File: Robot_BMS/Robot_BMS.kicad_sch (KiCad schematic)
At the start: 0 parts

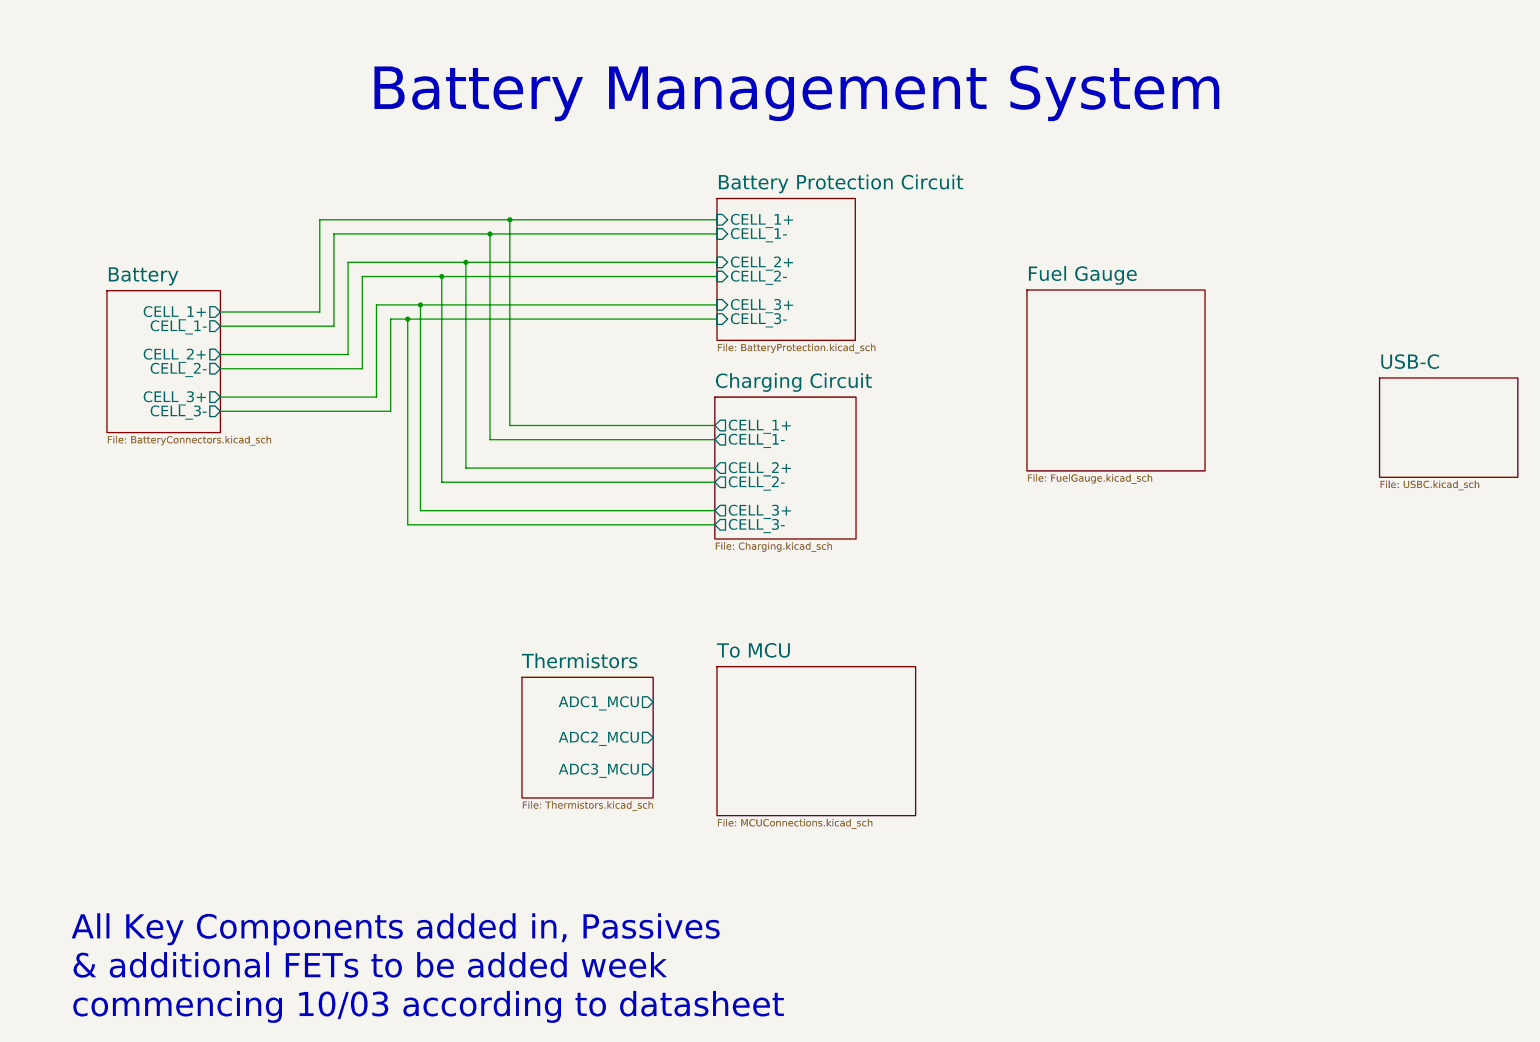
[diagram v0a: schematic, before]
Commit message: DC power supply added via dc Barrel jack
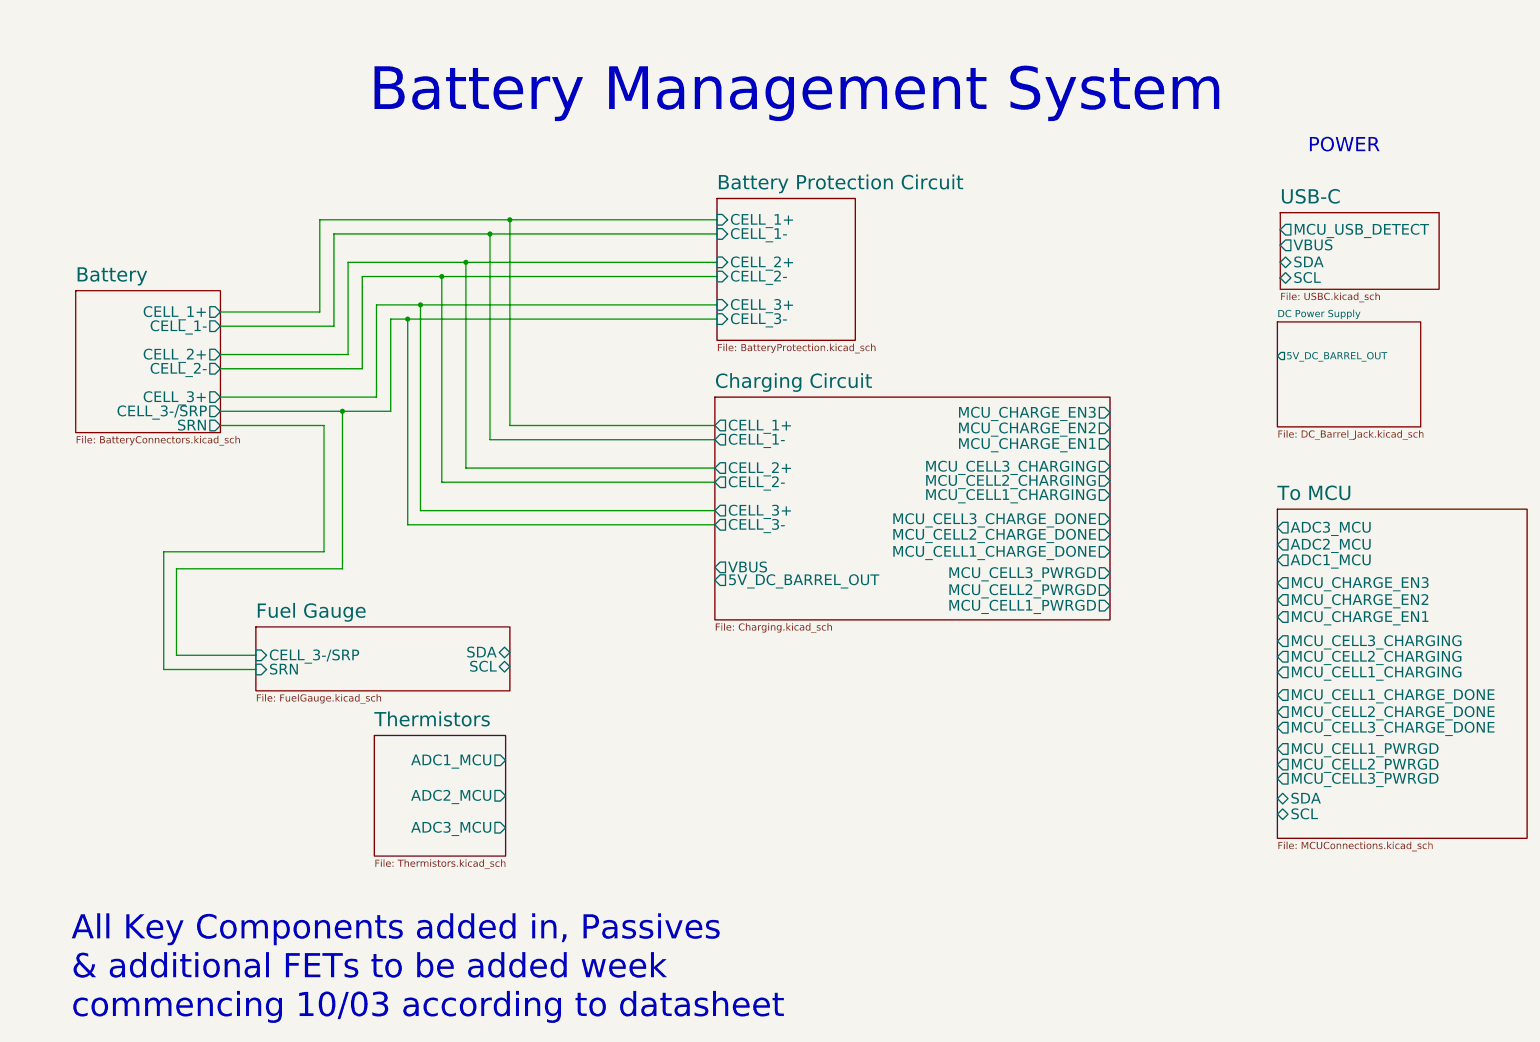
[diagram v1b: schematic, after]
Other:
- added sheet DC Power Supply (DC_Barrel_Jack.kicad_sch)
- sheet Battery ports: added CELL_3-/SRP, SRN; removed CELL_3-
- sheet Charging Circuit ports: added 5V_DC_BARREL_OUT, MCU_CELL1_CHARGE_DONE, MCU_CELL1_CHARGING, MCU_CELL1_PWRGD, MCU_CELL2_CHARGE_DONE, MCU_CELL2_CHARGING, MCU_CELL2_PWRGD, MCU_CELL3_CHARGE_DONE, MCU_CELL3_CHARGING, MCU_CELL3_PWRGD, MCU_CHARGE_EN1, MCU_CHARGE_EN2, MCU_CHARGE_EN3, VBUS; removed none
- sheet Fuel Gauge ports: added CELL_3-/SRP, SCL, SDA, SRN; removed none
- sheet To MCU ports: added ADC1_MCU, ADC2_MCU, ADC3_MCU, MCU_CELL1_CHARGE_DONE, MCU_CELL1_CHARGING, MCU_CELL1_PWRGD, MCU_CELL2_CHARGE_DONE, MCU_CELL2_CHARGING, MCU_CELL2_PWRGD, MCU_CELL3_CHARGE_DONE, MCU_CELL3_CHARGING, MCU_CELL3_PWRGD, MCU_CHARGE_EN1, MCU_CHARGE_EN2, MCU_CHARGE_EN3, SCL, SDA; removed none
- sheet USB-C ports: added MCU_USB_DETECT, SCL, SDA, VBUS; removed none
- note added: "POWER"

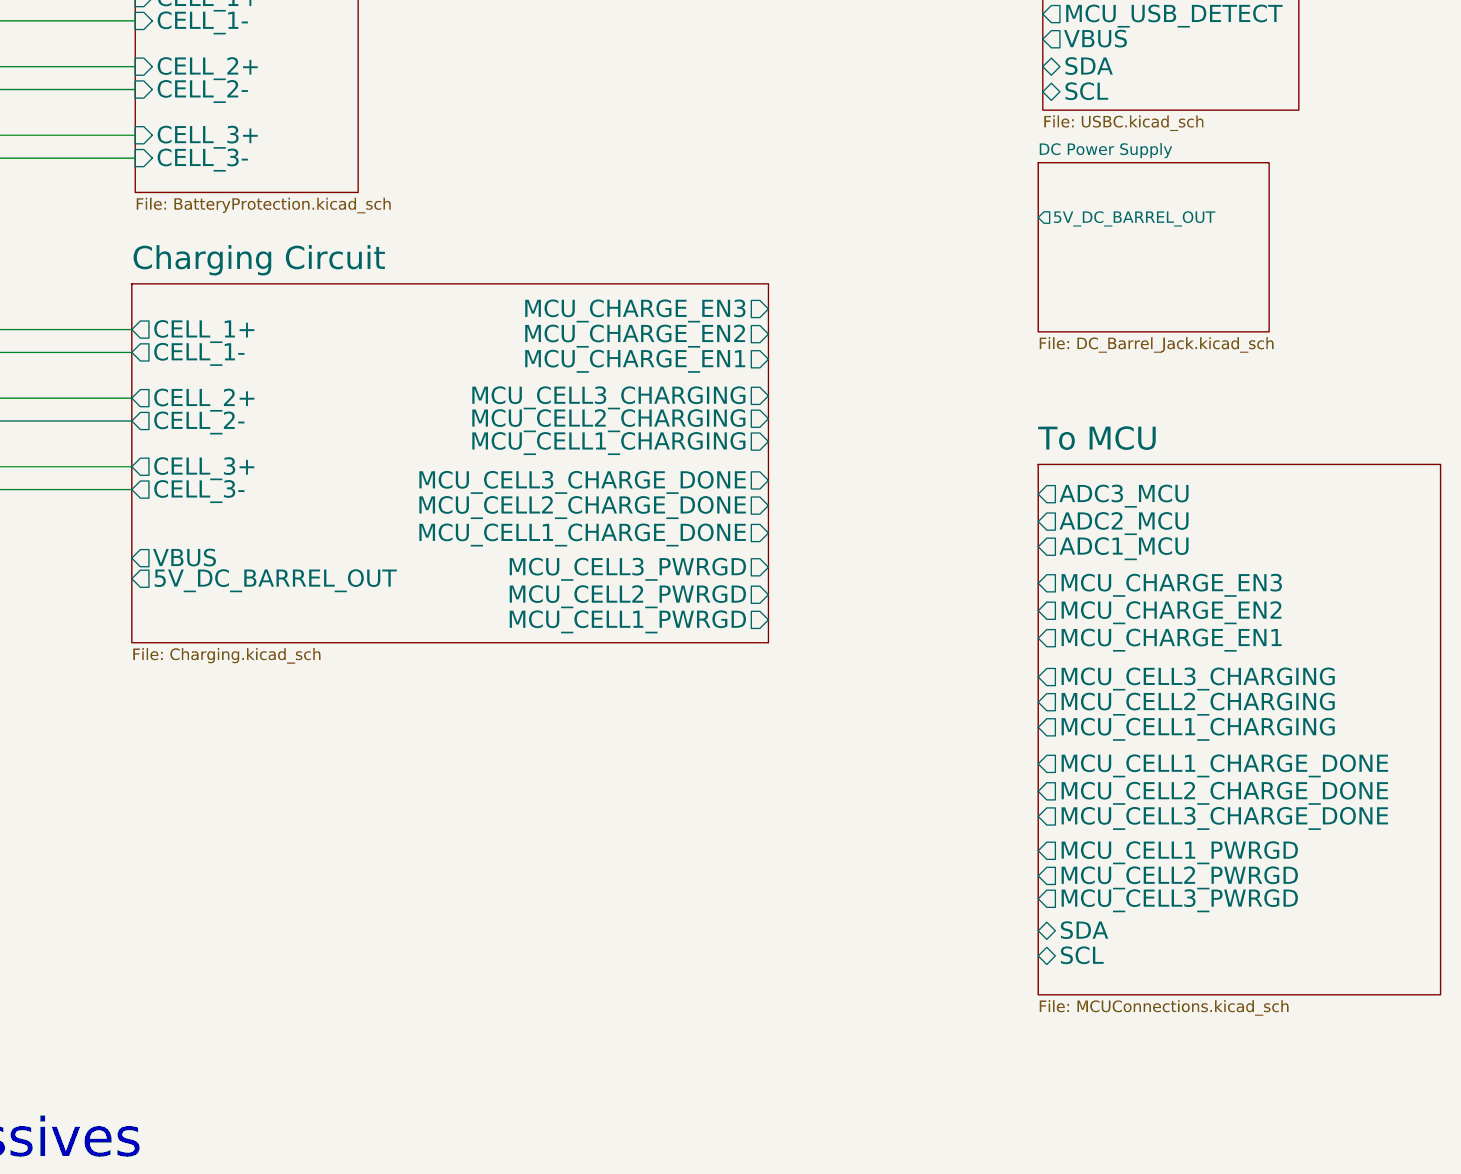
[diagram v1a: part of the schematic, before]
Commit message: implementing sepic converter for Solar power input
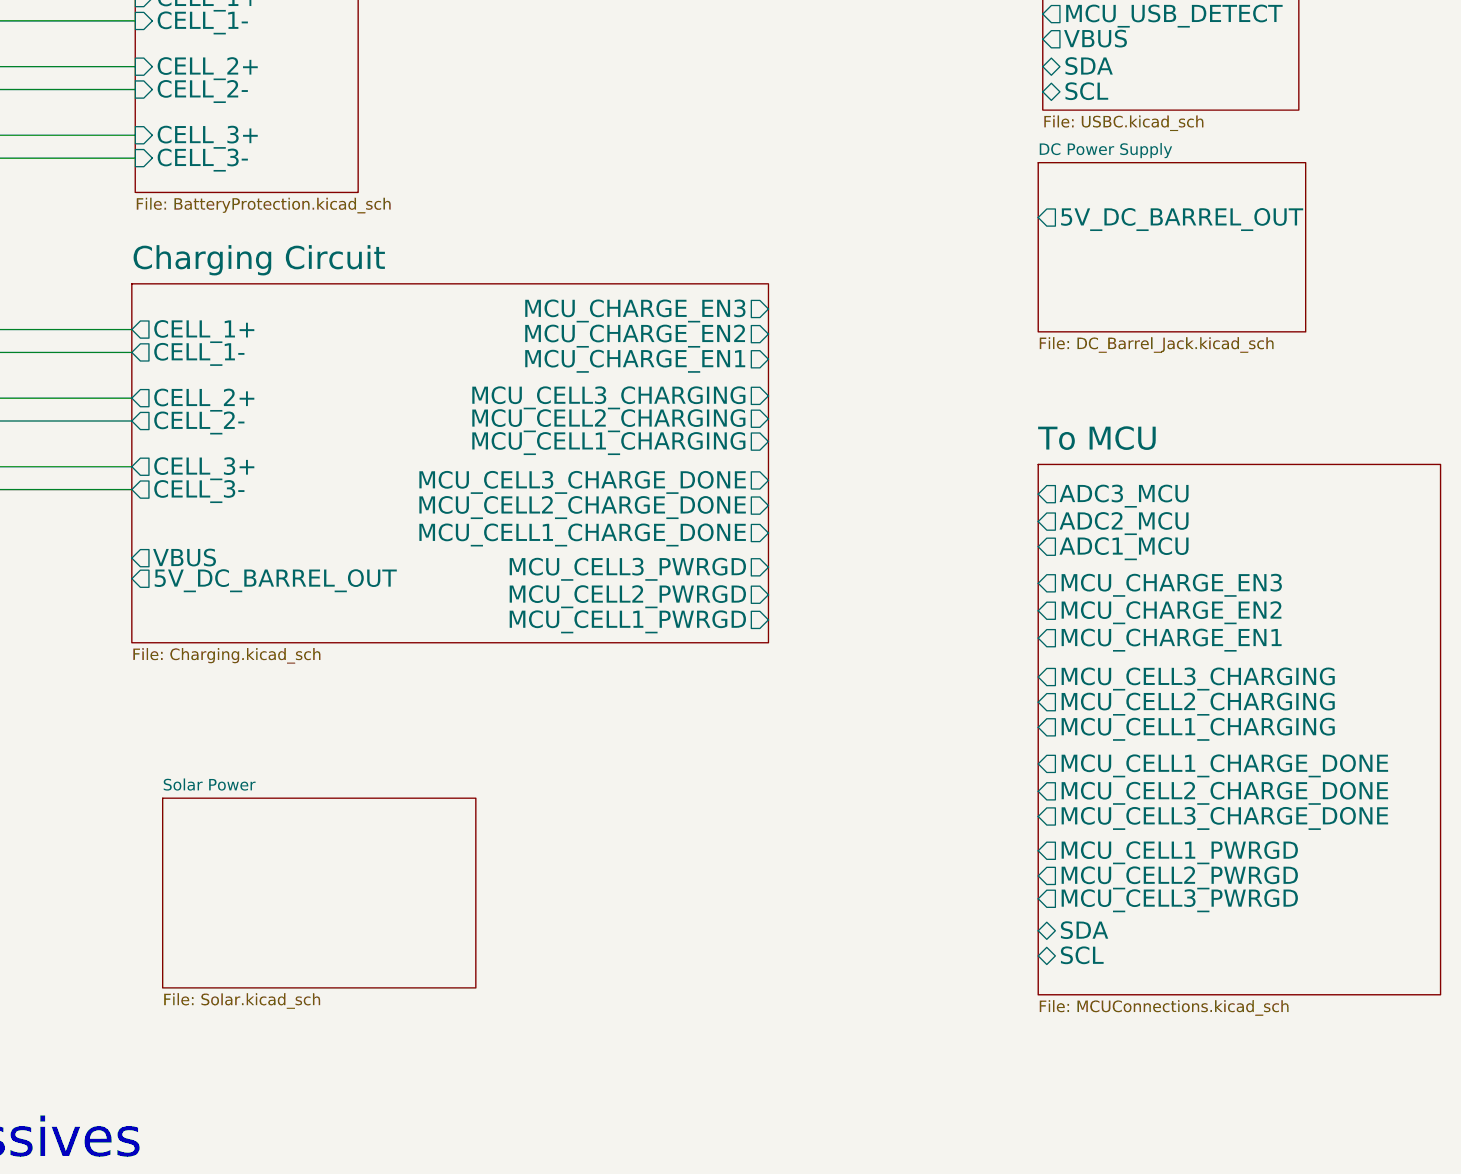
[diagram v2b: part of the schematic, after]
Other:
- added sheet Solar Power (Solar.kicad_sch)
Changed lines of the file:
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@@
 	(sheet
 		(at 229.87 69.088)
-		(size 25.654 18.796)
+		(size 29.718 18.796)
 		(fields_autoplaced yes)
 		(stroke
@@
 			(effects
 				(font
-					(size 1.27 1.27)
+					(size 1.905 1.905)
 				)
 				(justify left)
@@
 		)
 		(fill
-			(color 244 255 52 1.0000)
+			(color 88 0 0 1.0000)
 		)
 		(property "Sheetname" "USB-C"
@@
 				(font
 					(size 1.905 1.905)
+					(color 255 250 246 1)
 				)
 				(justify left)
@@
 				(font
 					(size 1.905 1.905)
+					(color 248 255 248 1)
 				)
 				(justify left)
@@
 				(font
 					(size 1.905 1.905)
+					(color 249 255 253 1)
 				)
 				(justify left)
@@
 				(font
 					(size 1.905 1.905)
+					(color 255 255 255 1)
 				)
 				(justify left)
@@
 				)
 			)
+		)
+	)
+	(sheet
+		(at 132.588 139.7)
+		(size 34.798 21.082)
+		(fields_autoplaced yes)
+		(stroke
+			(width 0.1524)
+			(type solid)
+		)
+		(fill
+			(color 255 255 11 1.0000)
+		)
+		(property "Sheetname" "Solar Power"
+			(at 132.588 138.9884 0)
+			(effects
+				(font
+					(size 1.27 1.27)
+				)
+				(justify left bottom)
+			)
+		)
+		(property "Sheetfile" "Solar.kicad_sch"
+			(at 132.588 161.3666 0)
+			(effects
+				(font
+					(size 1.27 1.27)
+				)
+				(justify left top)
+			)
+		)
+		(instances
+			(project "Robot_BMS"
+				(path "/72551b1c-3d40-4199-8911-e5b015f4abec"
+					(page "10")
+				)
+			)

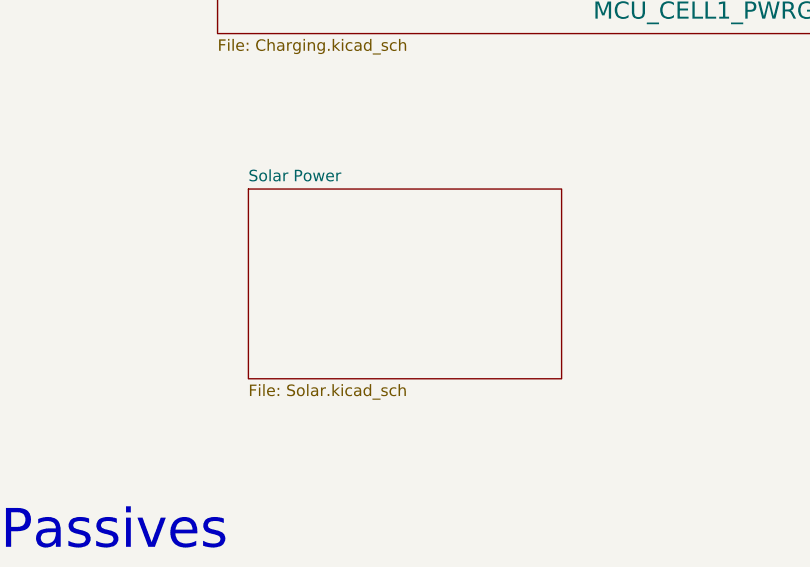
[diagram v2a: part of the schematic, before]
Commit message: USB-c PD to 15V
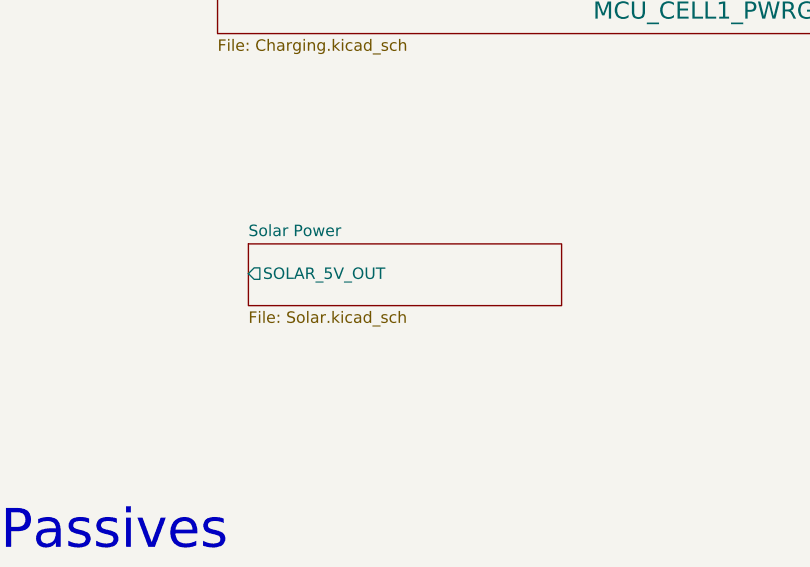
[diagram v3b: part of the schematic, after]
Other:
- sheet Solar Power ports: added SOLAR_5V_OUT; removed none
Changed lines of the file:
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@@
 	)
 	(sheet
-		(at 132.588 139.7)
-		(size 34.798 21.082)
+		(at 132.588 145.796)
+		(size 34.798 6.858)
 		(fields_autoplaced yes)
 		(stroke
@@
 		)
 		(property "Sheetname" "Solar Power"
-			(at 132.588 138.9884 0)
+			(at 132.588 145.0844 0)
 			(effects
 				(font
@@
 		)
 		(property "Sheetfile" "Solar.kicad_sch"
-			(at 132.588 161.3666 0)
+			(at 132.588 153.2386 0)
 			(effects
 				(font
@@
 			)
 		)
+		(pin "SOLAR_5V_OUT" output
+			(at 132.588 149.098 180)
+			(effects
+				(font
+					(size 1.27 1.27)
+				)
+				(justify left)
+			)
+		)
